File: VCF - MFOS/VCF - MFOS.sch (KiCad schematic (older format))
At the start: 73 parts, among them J1 CV3, J2 AudioIn1, J3 AudioIn2, J4 AudioIn3, J5 CV1, J6 CV2, J7 AudioOut, Q1 2N3906, Q2 2N3906, Q3 2N3906, Q4 2N3904, Q5 2N3904, Q6 2N3906, U1 LM13700, U2 TL084, U3 TL082, U4 TL082, U5 LM13700

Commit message: VCF
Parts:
- removed 0.1uF1: CP1, symbol Device:CP1
- removed C1: 0.1uF, symbol Device:CP1
- removed C7, C8: 100pF, symbol Device:CP1
- removed D1: D, symbol Device:D
- removed J1: CV3, symbol Connector:AudioJack2
- removed J2: AudioIn1, symbol Connector:AudioJack2
- removed J3: AudioIn2, symbol Connector:AudioJack2
- removed J4: AudioIn3, symbol Connector:AudioJack2
- removed J5: CV1, symbol Connector:AudioJack2
- removed J6: CV2, symbol Connector:AudioJack2
- removed J7: AudioOut, symbol Connector:AudioJack2
- removed R19, R2, R35, R39, R42: 100K, symbol Device:R_US
- removed R34: 1M, symbol Device:R_US
- removed R36, R43: 100, symbol Device:R_US
- removed R37: 2K, symbol Device:R_US
- removed R38: 20K, symbol Device:R_US
- removed R40: 43K, symbol Device:R_US
- removed R41: 10K, symbol Device:R_US
- removed RV1: 100K, symbol Device:R_POT_US
- removed RV2: 100, symbol Device:R_POT_US
- removed U1, U5: LM13700, symbol Amplifier_Operational:LM13700
- removed U2: TL084, symbol Amplifier_Operational:TL084
- removed U4: TL082, symbol Amplifier_Operational:TL082
- added C15, C16, C17, C18: 1uF, symbol Device:CP1
- added D1: 1N914, Diode_THT:D_DO-35_SOD27_P7.62mm_Horizontal, symbol Diode:1N914
- added J1: AIN1, symbol Connector:Conn_01x01_Female
- added J10: FOUT, symbol Connector:Conn_01x01_Female
- added J2: AIN2, symbol Connector:Conn_01x01_Female
- added J3: AIN3, symbol Connector:Conn_01x01_Female
- added J4: CV1, symbol Connector:Conn_01x01_Female
- added J5: CV2, symbol Connector:Conn_01x01_Female
- added J6: CV3, symbol Connector:Conn_01x01_Female
- added J7: CO3, symbol Connector:Conn_01x01_Female
- added J8: CO2, symbol Connector:Conn_01x01_Female
- added J9: C01, symbol Connector:Conn_01x01_Female
- added R19: 100, symbol Device:R_POT_US
- added R2: 100K, symbol Device:R_POT_US
- added R51, R56, R58, R59, R60, R62: 100K, symbol Device:R_US
- added R52, R53, R54: 1M, symbol Device:R_US
- added R55: 390K, symbol Device:R_US
- added R57: 4.7M, symbol Device:R_US
- added R61: 2K, symbol Device:R_US
- added U1: TL084, symbol Amplifier_Operational:TL084
- added U2, U4: LM13700, symbol Amplifier_Operational:LM13700
- added U8: TL082, symbol Amplifier_Operational:TL082
- C2, C3: value 0.1uF -> 100pF
- R1: value 20K -> 39K
- R10, R21, R29: value 100K -> 39K
- R11: value 100K -> 33K
- R12: value 1M -> 100K
- R13: value 1M -> 39K
- R14: value 1M -> 2K
- R15: value 10K -> 20K
- R16: value 2K -> 100
- R17: value 390K -> 100K
- R18: value 20K -> 10K
- R20: value 39K -> 475
- R22: value 100 -> 20K
- R23: value 475 -> 47K
- R24, R31: value 10K -> 100
- R25: value 4.7M -> 100K
- R26, R28, R9: value 100K -> 10K
- R27: value 20K -> 1M
- R3: value 39K -> 20K
- R30: value 47K -> 20K
- R32: value 43K -> 100K
- R4: value 33K -> 100
- R5: value 39K -> 100K
- R7: value 100 -> 100K
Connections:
- net +12V: now also R11.2, R15.2, R22.2, R3.2, R30.2, U1.4 (V+), U2.11 (V+), U4.11 (V+), U8.8 (V+); no longer R1.2, R18.2, R4.1
- net -12V: now also R1.1, R10.1, R13.1, R21.1, R29.1, U1.11 (V-), U2.6 (V-), U4.6 (V-), U8.4 (V-); no longer R20.1, R3.1, R32.1, R5.1
- net Earth: now also C2.2, C3.2, C6.2, R16.1, R20.2, R24.1, R31.1, R4.1, R57.1, R58.2, U2.14 (+), U2.3 (+), U4.14 (+), U4.3 (+), U8.3 (+), U8.5 (+); no longer C4.2, R22.1, R23.2, R25.1, R26.2, R7.1
- net RA: now also R59.1, R61.2, U8.7; no longer R29.1
- net RB: now also R1.2, R4.2, R5.2, R51.1, U2.13 (-); no longer R3.2, R6.2, R7.2
- net at R9.2: now also Q1.3 (C)
- net at R8.2: now also J6.1 (Pin_1)
- net at R10.2: now also J9.1 (Pin_1), R2.3
- net at Q4.3 (C), U3.6 (-): now also C4.2, R27.1; no longer C6.2
- net at Q4.2 (B): now also D1.2 (A), R19.2
- net at R23.1: now also C4.1, R26.2, U3.7
- net at Q4.1 (E), Q5.1 (E): now also R26.1; no longer R31.1
- net at R15.1: now also U2.2 (DIODE_BIAS)
- net at R18.1: now also U2.1
- net at C5.1: now also U1.10 (+), U4.12
- net at R28.1: now also U4.16; no longer R32.2
- net at R33.1: now also U4.1
- net at R28.2: now also Q3.3 (C); no longer R21.1
- net at R6.1: now also J4.1 (Pin_1)
- net at U3.1: now also R14.1, R19.1; no longer R17.1
- net at R25.2: now also R21.2, R24.2, R60.1, U4.13 (-)
- net at R29.2: now also R31.2, R32.2, R62.1, U4.4 (-); no longer R26.1
- net at R12.2: now also J8.1 (Pin_1), R2.2
- net at C2.1: now also U1.3 (+), U2.12; no longer R13.2
- net at R14.2: now also R12.1, R6.2, R7.1, R8.1, U3.2 (-); no longer C3.1
- net at Q2.3 (C): now also R18.2; no longer R24.2
- net at R33.2: now also Q6.3 (C); no longer Q3.3 (C)
- new net: J7.1 (Pin_1), R11.1, R2.1
- new net: J5.1 (Pin_1), R7.2
- new net: R19.3, R20.1
- new net: D1.1 (K), R23.2
- new net: R9.1, U2.16
- new net: R3.1, U2.15 (DIODE_BIAS)
- new net: R5.1, R56.2, U1.1, U1.2 (-)
- new net: R13.2, R16.2, R17.2, R56.1, U2.4 (-)
- new net: C3.1, U1.5 (+), U2.5
- new net: R17.1, R60.2, U1.6 (-), U1.7
- new net: R22.1, U4.15 (DIODE_BIAS)
- new net: R25.1, R62.2, U1.8, U1.9 (-)
- new net: R30.1, U4.2 (DIODE_BIAS)
- new net: C6.1, U1.12 (+), U4.5
- new net: C18.1, R32.1, U1.13 (-), U1.14
- new net: R51.2, R55.1, U8.1
- new net: C15.2, J1.1 (Pin_1)
- new net: C16.2, J2.1 (Pin_1)
- new net: C17.2, J3.1 (Pin_1)
- new net: C15.1, R52.1
- new net: R52.2, R53.2, R54.2, R55.2, U8.2 (-)
- new net: C16.1, R53.1
- new net: C17.1, R54.1
- new net: C18.2, R57.2, R58.1, R59.2, U8.6 (-)
- new net: J10.1 (Pin_1), R61.1

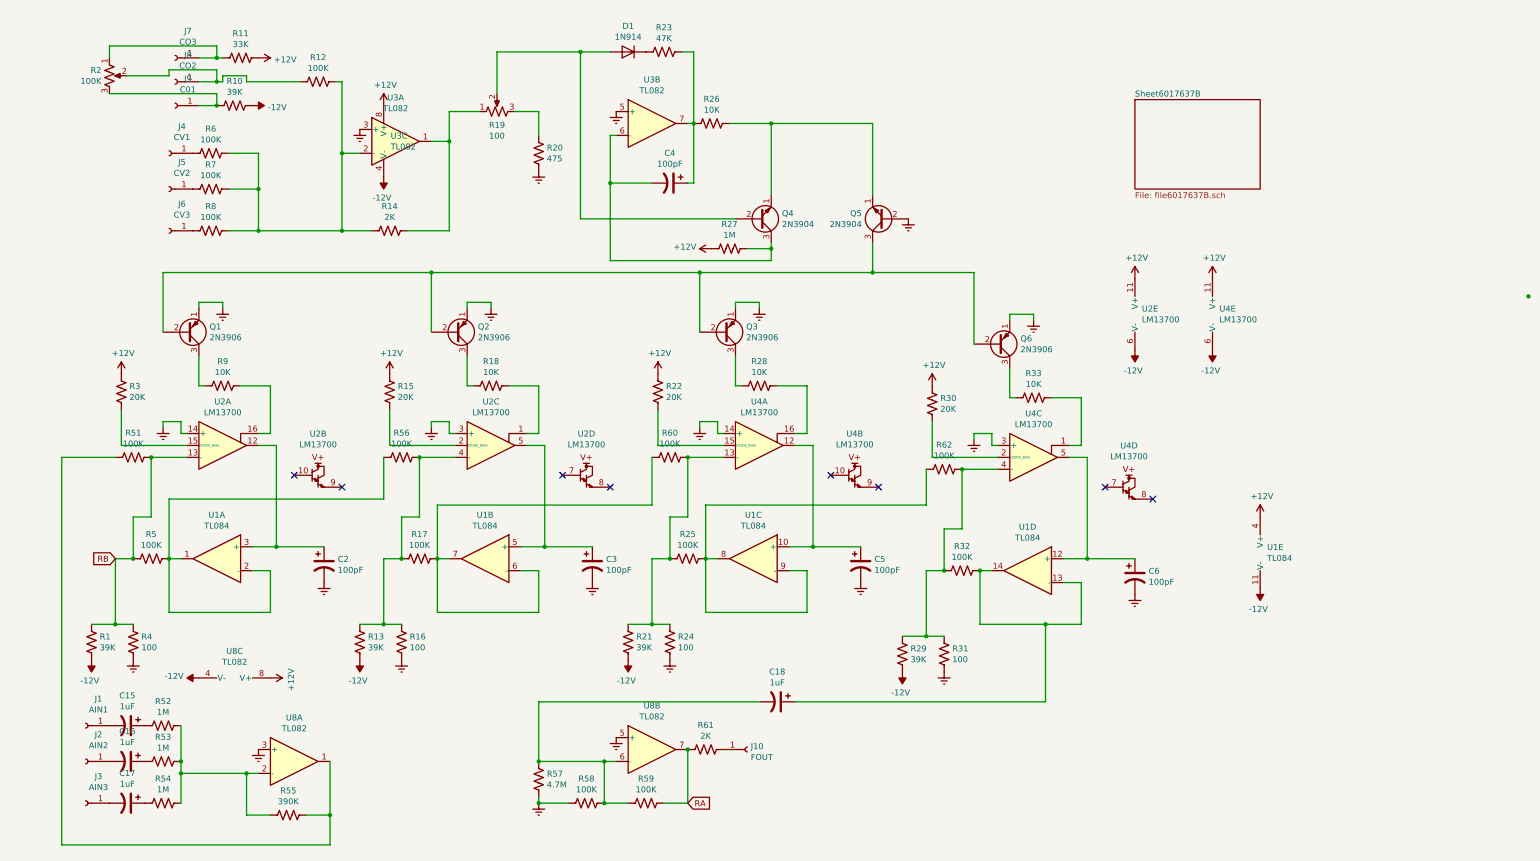
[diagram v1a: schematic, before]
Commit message: fixed some incorrect component values
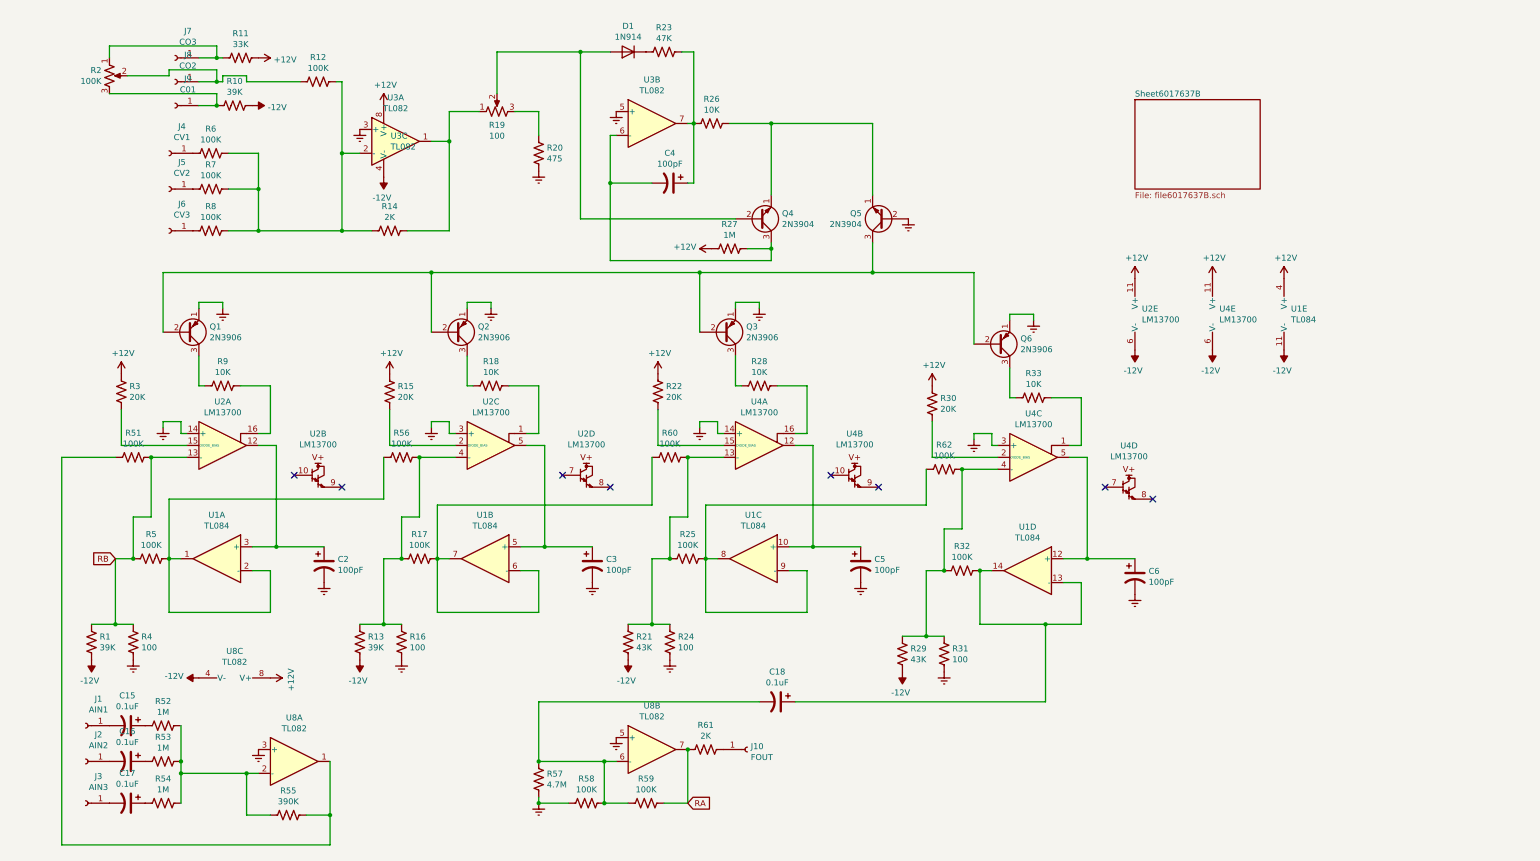
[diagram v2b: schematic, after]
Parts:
- C15, C16, C17, C18: value 1uF -> 0.1uF
- R21, R29: value 39K -> 43K
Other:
- moved on the sheet: U1E
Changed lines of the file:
@@
 EESchema Schematic File Version 4
-EELAYER 30 0
+LIBS:VCF - MFOS-cache
+EELAYER 29 0
 EELAYER END
 $Descr A4 11693 8268
@@
 P 5350 5950
 F 0 "R21" H 5282 5904 50  0000 R CNN
-F 1 "39K" H 5282 5995 50  0000 R CNN
+F 1 "43K" H 5282 5995 50  0000 R CNN
 F 2 "" V 5280 5950 50  0001 C CNN
 F 3 "~" H 5350 5950 50  0001 C CNN
@@
 P 7650 6050
 F 0 "R29" H 7582 6004 50  0000 R CNN
-F 1 "39K" H 7582 6095 50  0000 R CNN
+F 1 "43K" H 7582 6095 50  0000 R CNN
 F 2 "" V 7580 6050 50  0001 C CNN
 F 3 "~" H 7650 6050 50  0001 C CNN
@@
 L Amplifier_Operational:TL084 U1
 U 5 1 6014C3CF
-P 10750 5200
-F 0 "U1" H 10708 5246 50  0000 L CNN
-F 1 "TL084" H 10708 5155 50  0000 L CNN
-F 2 "" H 10700 5300 50  0001 C CNN
-F 3 "http://www.ti.com/lit/ds/symlink/tl081.pdf" H 10800 5400 50  0001 C CNN
-	5    10750 5200
+P 10950 3200
+F 0 "U1" H 10908 3246 50  0000 L CNN
+F 1 "TL084" H 10908 3155 50  0000 L CNN
+F 2 "" H 10900 3300 50  0001 C CNN
+F 3 "http://www.ti.com/lit/ds/symlink/tl081.pdf" H 11000 3400 50  0001 C CNN
+	5    10950 3200
 	1    0    0    -1
 $EndComp
@@
 L power:+12V #PWR038
 U 1 1 6014E989
-P 10650 4900
-F 0 "#PWR038" H 10650 4750 50  0001 C CNN
-F 1 "+12V" H 10665 5073 50  0000 C CNN
-F 2 "" H 10650 4900 50  0001 C CNN
-F 3 "" H 10650 4900 50  0001 C CNN
-	1    10650 4900
+P 10850 2900
+F 0 "#PWR038" H 10850 2750 50  0001 C CNN
+F 1 "+12V" H 10865 3073 50  0000 C CNN
+F 2 "" H 10850 2900 50  0001 C CNN
+F 3 "" H 10850 2900 50  0001 C CNN
+	1    10850 2900
 	1    0    0    -1
 $EndComp
@@
 L power:-12V #PWR039
 U 1 1 6014F324
-P 10650 5500
-F 0 "#PWR039" H 10650 5600 50  0001 C CNN
-F 1 "-12V" H 10665 5673 50  0000 C CNN
-F 2 "" H 10650 5500 50  0001 C CNN
-F 3 "" H 10650 5500 50  0001 C CNN
-	1    10650 5500
+P 10850 3500
+F 0 "#PWR039" H 10850 3600 50  0001 C CNN
+F 1 "-12V" H 10865 3673 50  0000 C CNN
+F 2 "" H 10850 3500 50  0001 C CNN
+F 3 "" H 10850 3500 50  0001 C CNN
+	1    10850 3500
 	-1   0    0    1
 $EndComp
@@
 P 1150 6650
 F 0 "C15" V 898 6650 50  0000 C CNN
-F 1 "1uF" V 989 6650 50  0000 C CNN
+F 1 "0.1uF" V 989 6650 50  0000 C CNN
 F 2 "" H 1150 6650 50  0001 C CNN
 F 3 "~" H 1150 6650 50  0001 C CNN
@@
 P 1150 6950
 F 0 "C16" V 898 6950 50  0000 C CNN
-F 1 "1uF" V 989 6950 50  0000 C CNN
+F 1 "0.1uF" V 989 6950 50  0000 C CNN
 F 2 "" H 1150 6950 50  0001 C CNN
 F 3 "~" H 1150 6950 50  0001 C CNN
@@
 P 1150 7300
 F 0 "C17" V 898 7300 50  0000 C CNN
-F 1 "1uF" V 989 7300 50  0000 C CNN
+F 1 "0.1uF" V 989 7300 50  0000 C CNN
 F 2 "" H 1150 7300 50  0001 C CNN
 F 3 "~" H 1150 7300 50  0001 C CNN
@@
 P 6600 6450
 F 0 "C18" V 6348 6450 50  0000 C CNN
-F 1 "1uF" V 6439 6450 50  0000 C CNN
+F 1 "0.1uF" V 6439 6450 50  0000 C CNN
 F 2 "" H 6600 6450 50  0001 C CNN
 F 3 "~" H 6600 6450 50  0001 C CNN
@@
 Wire Wire Line
 	3700 2850 5950 2850
-Connection ~ 12900 3050
 $EndSCHEMATC
